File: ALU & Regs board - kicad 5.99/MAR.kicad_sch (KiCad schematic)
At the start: 8 parts, among them U47 MC74ACT273DWG, U48 MC74ACT273DWG, U49 MC74ACT244DWG, U50 MC74ACT244DWG

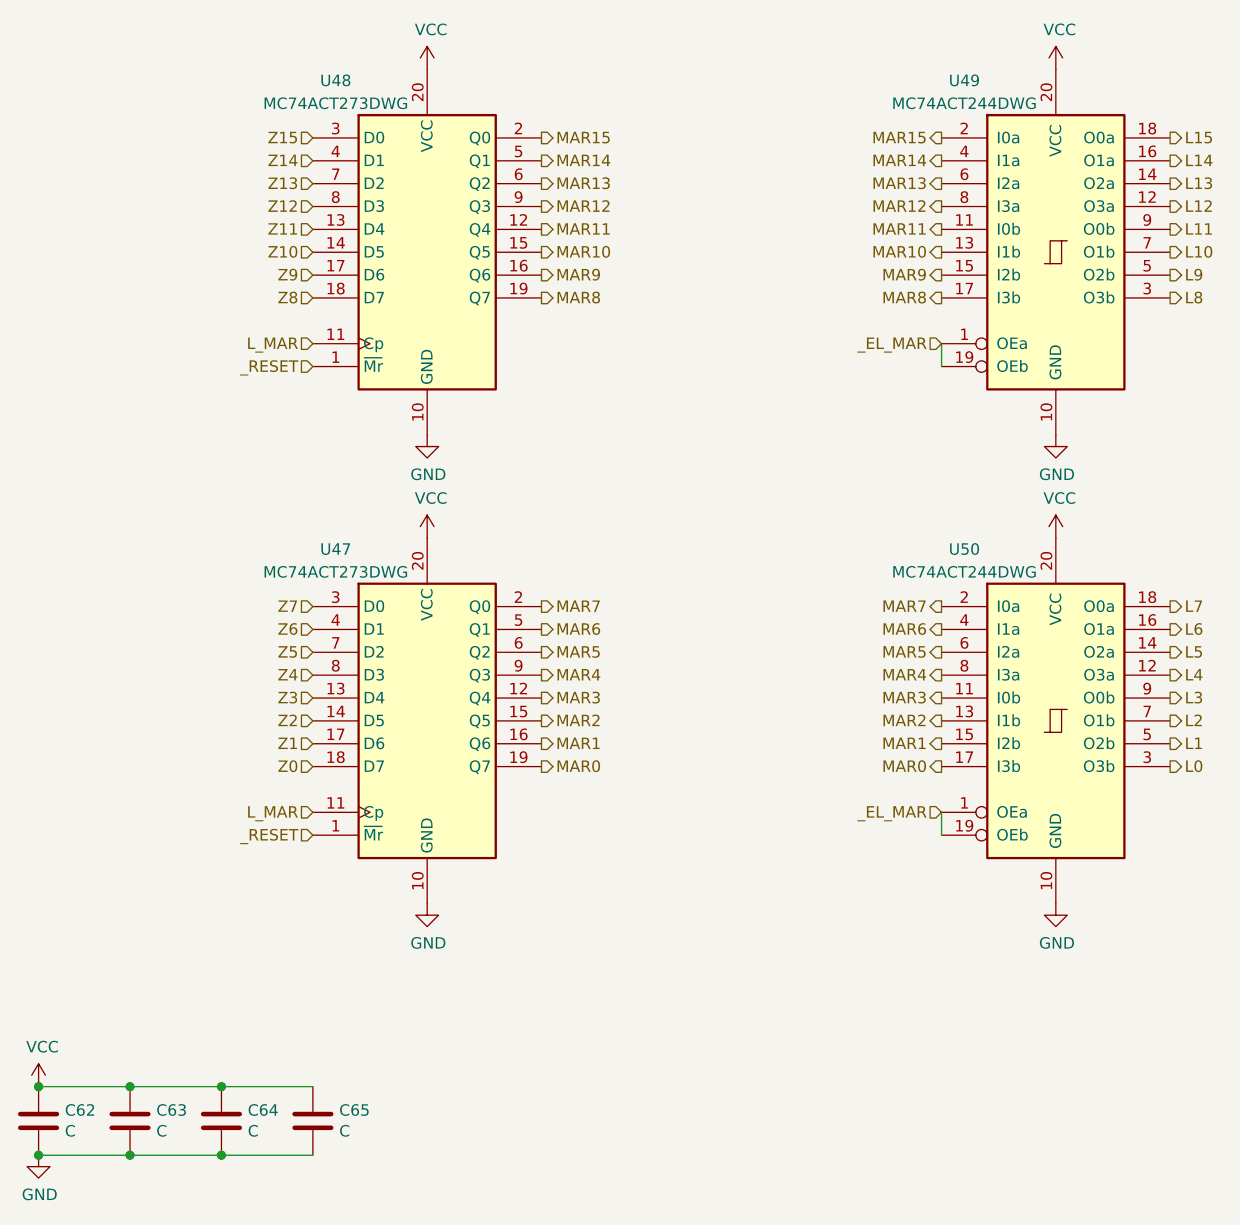
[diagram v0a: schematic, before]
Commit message: added a buffer on the _RESET line, which is rather loaded
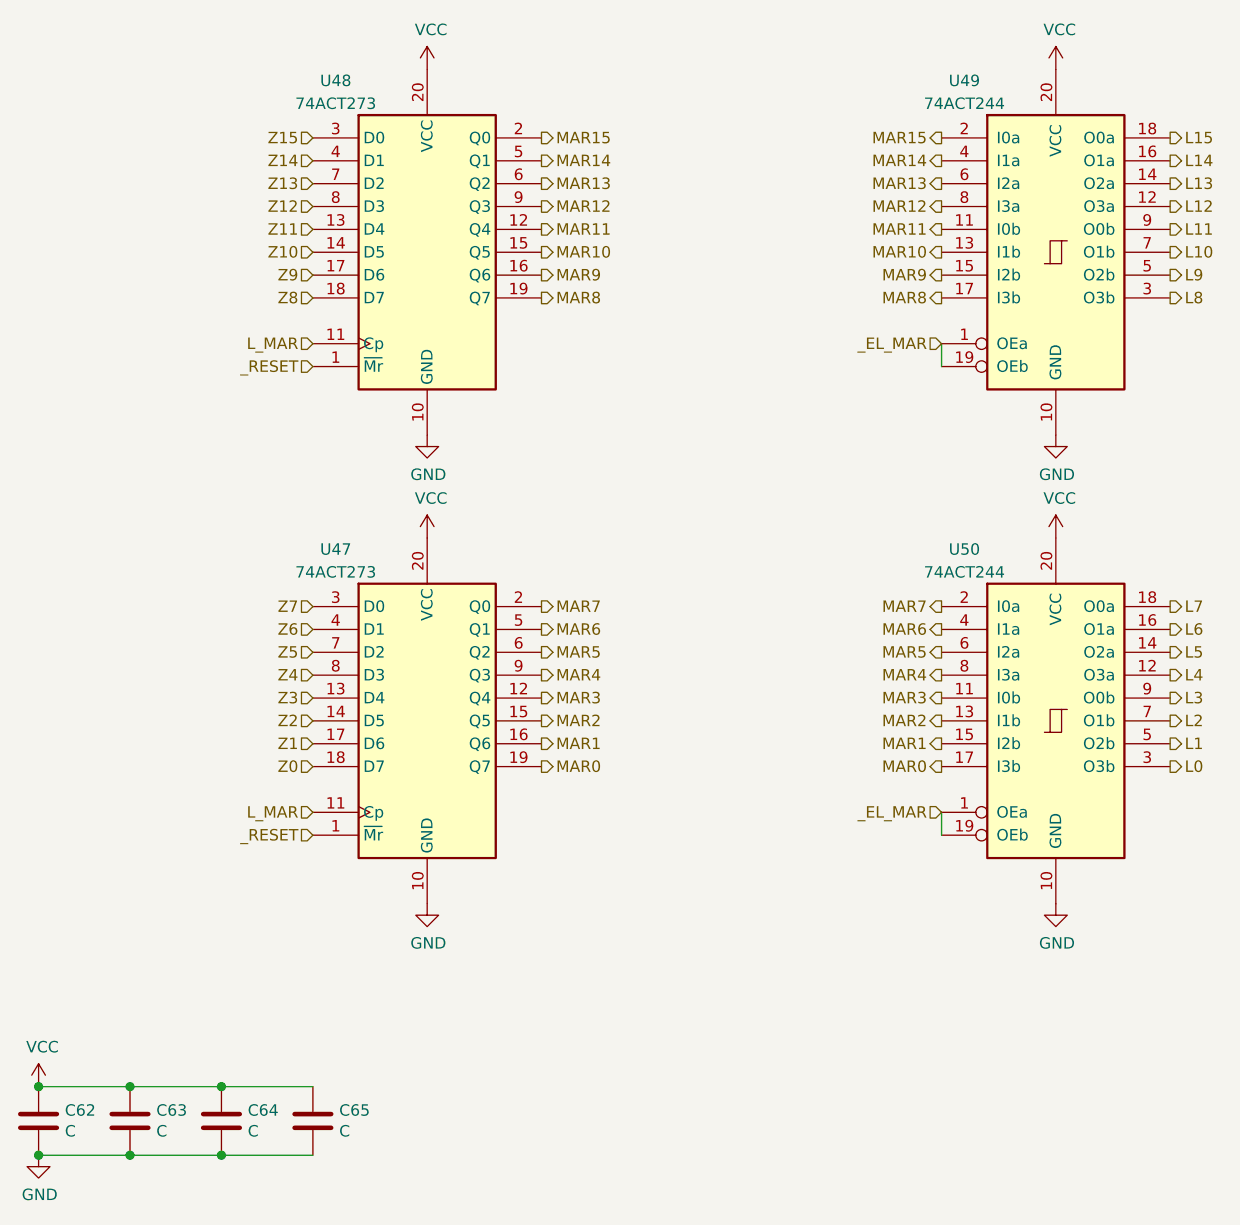
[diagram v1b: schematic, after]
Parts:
- U47, U48: value MC74ACT273DWG -> 74ACT273
- U49, U50: value MC74ACT244DWG -> 74ACT244
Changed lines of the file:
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@@
     (in_bom yes) (on_board yes)
     (property "Reference" "U48" (id 0) (at 76.2 50.8 0))
-    (property "Value" "MC74ACT273DWG" (id 1) (at 76.2 53.34 0))
+    (property "Value" "74ACT273" (id 1) (at 76.2 53.34 0))
     (property "Footprint" "Package_SO:SOIC-20W_7.5x12.8mm_P1.27mm" (id 2) (at 86.36 69.85 0)
       (effects (font (size 1.27 1.27)) hide)
@@
     (in_bom yes) (on_board yes)
     (property "Reference" "U47" (id 0) (at 76.2 102.87 0))
-    (property "Value" "MC74ACT273DWG" (id 1) (at 76.2 105.41 0))
+    (property "Value" "74ACT273" (id 1) (at 76.2 105.41 0))
     (property "Footprint" "Package_SO:SOIC-20W_7.5x12.8mm_P1.27mm" (id 2) (at 86.36 121.92 0)
       (effects (font (size 1.27 1.27)) hide)
@@
     (in_bom yes) (on_board yes)
     (property "Reference" "U49" (id 0) (at 146.05 50.8 0))
-    (property "Value" "MC74ACT244DWG " (id 1) (at 146.05 53.34 0))
+    (property "Value" "74ACT244" (id 1) (at 146.05 53.34 0))
     (property "Footprint" "Package_SO:SOIC-20W_7.5x12.8mm_P1.27mm" (id 2) (at 156.21 69.85 0)
       (effects (font (size 1.27 1.27)) hide)
@@
     (in_bom yes) (on_board yes)
     (property "Reference" "U50" (id 0) (at 146.05 102.87 0))
-    (property "Value" "MC74ACT244DWG " (id 1) (at 146.05 105.41 0))
+    (property "Value" "74ACT244" (id 1) (at 146.05 105.41 0))
     (property "Footprint" "Package_SO:SOIC-20W_7.5x12.8mm_P1.27mm" (id 2) (at 156.21 121.92 0)
       (effects (font (size 1.27 1.27)) hide)
